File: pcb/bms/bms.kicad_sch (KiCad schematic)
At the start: 11 parts, among them J1 Analog, J2 Digital, Q1 IRF3205, Q2 IRF3205, U1 LM358

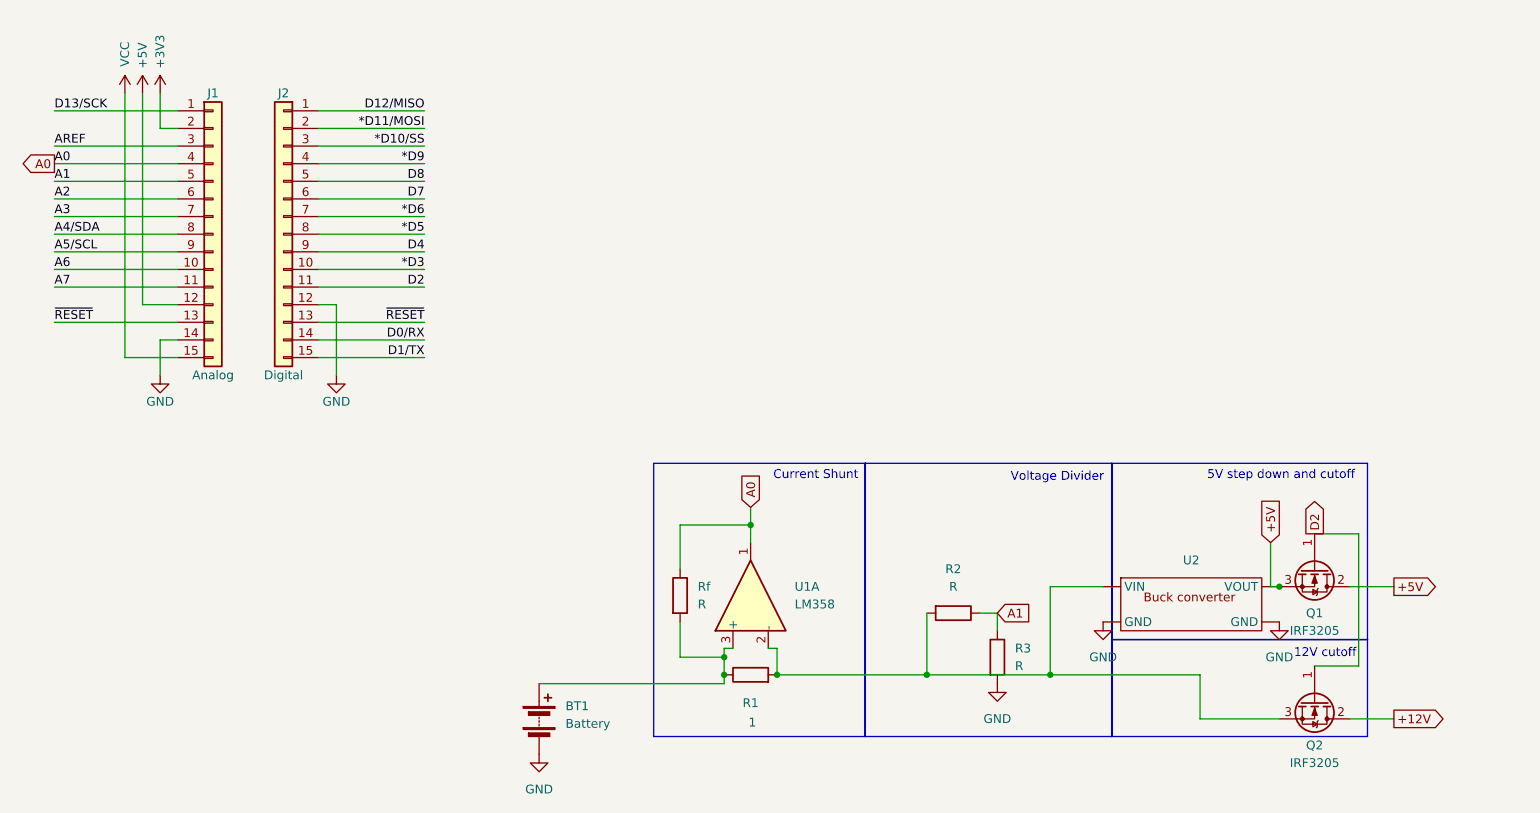
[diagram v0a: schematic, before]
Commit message: Finish documentation
Added demo videos and presentations
Added descriptions and copyright info to code
Update schematic
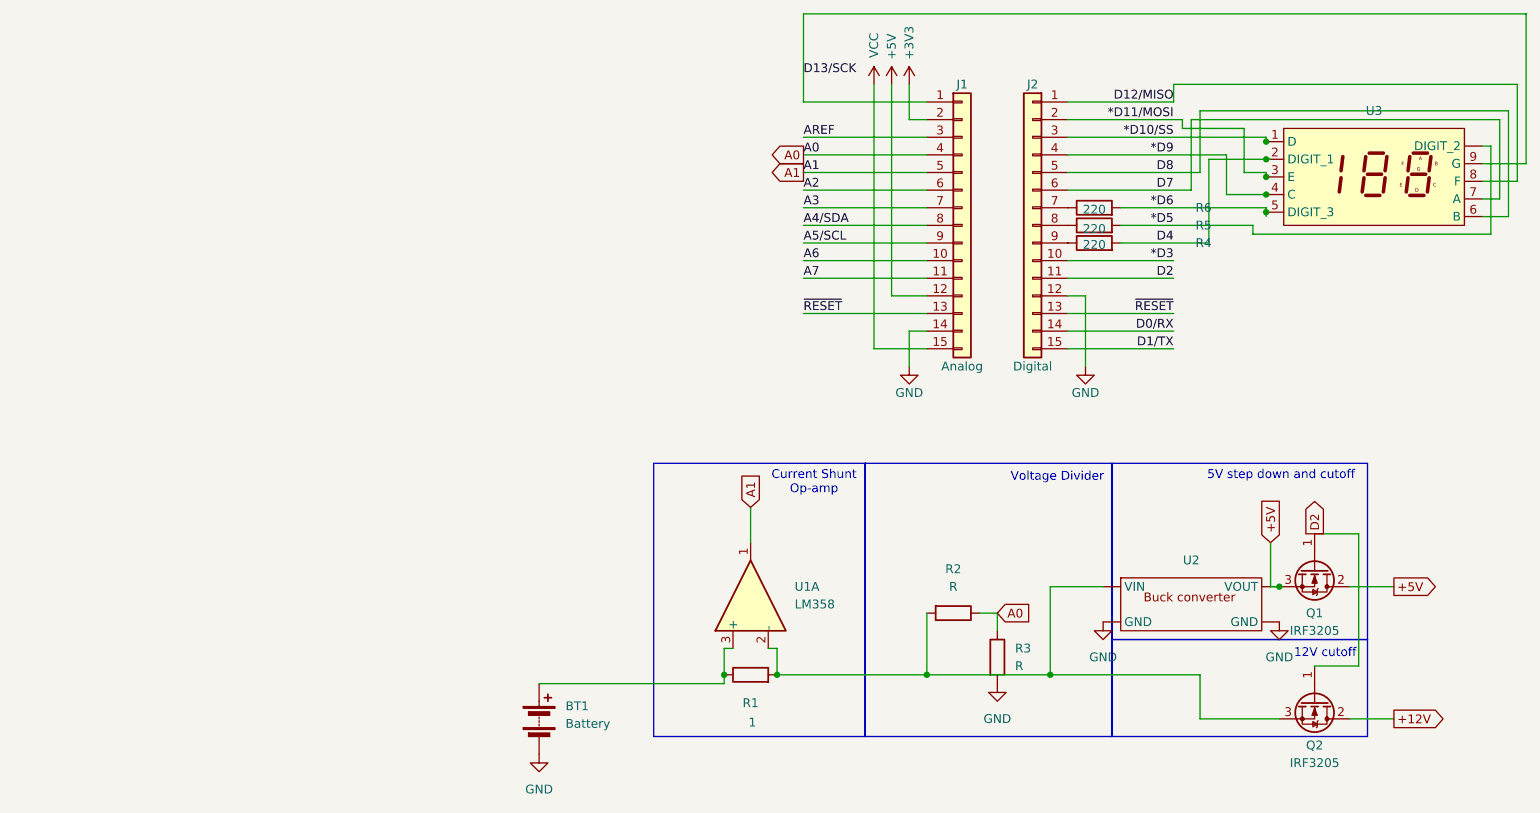
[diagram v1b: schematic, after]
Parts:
- removed Rf: R, symbol Device:R
- added R4, R5, R6: 220, symbol Device:R
- added U3: (no value), symbol New_Library_1led:E30401
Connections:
- net *D10/SS: now also U3.1 (D)
- net *D11/MOSI: now also U3.3 (E)
- net *D5: now also R5.2, U3. (DIGIT_2); no longer J2.8 (Pin_8)
- net *D6: now also R6.2, U3.5 (DIGIT_3); no longer J2.7 (Pin_7)
- net *D9: now also U3.4 (C)
- net A0: now also R2.1, R3.1; no longer U1.1
- net A1: now also U1.1; no longer R2.1, R3.1
- net D12/MISO: now also U3.8 (F)
- net D13/SCK: now also U3.9 (G)
- net D4: now also R4.2, U3.2 (DIGIT_1); no longer J2.9 (Pin_9)
- net D7: now also U3.7 (A)
- net D8: now also U3.6 (B)
- new net: J2.7 (Pin_7), R6.1
- new net: J2.8 (Pin_8), R5.1
- new net: J2.9 (Pin_9), R4.1
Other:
- note added: "Current Shunt Op-amp"
- note removed: "Current Shunt"
- moved on the sheet: J1, J2
